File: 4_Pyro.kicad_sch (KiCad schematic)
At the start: 27 parts, among them J601 XT60-M, Q601 IRLZ44N, Q602 IRLZ44N, Q603 IRLZ44N, Q604 IRLZ44N, Q605 IRLZ44N, Q606 IRLZ44N, U601 PC817, U602 PC817, U603 PC817, U604 PC817, U605 PC817, U606 PC817

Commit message: Continued connections for the new NAV
Added continuity sensing through a 8:1 mux
Restructured schematic so that everything actually fits in page 4
Updated CubeMX (ioc) file with pinout
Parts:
- added R505, R506, R511, R512, R517, R518: 4k7, symbol Device:R
- added R519: 1k, symbol Device:R
- added U507: CD4051B, Package_SO:SOIC-16_3.9x9.9mm_P1.27mm, symbol Analog_Switch:CD4051B
- renumbered C601 to C501, D601 to D501, J601 to J501, Q605 to Q501, Q602 to Q502, Q603 to Q503, Q604 to Q504, Q601 to Q505, Q606 to Q506, R609 to R501, R602 to R502, R611 to R503, R604 to R504, R605 to R507, R606 to R508, R607 to R509, R608 to R510, R601 to R513, R610 to R514, R603 to R515, R612 to R516, U605 to U501, U602 to U502, U603 to U503, U604 to U504, U601 to U505, U606 to U506
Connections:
- net DROGUE_S1 is gone; now on net PYRO_0: U501.1
- net DROGUE_S2 is gone; now on net PYRO_1: U502.1
- net FIRE_S1 is gone; now on net PYRO_2: U503.1
- net FIRE_S2 is gone; now on net PYRO_3: U504.1
- net MAIN_S1 is gone; now on net PYRO_4: U505.1
- net GND: now also R519.2; no longer C501.2, D501.1 (A1)
- net DROGUE_1 renamed PYRO_0
- net PYRO_0: now also R505.1, R505.2, U507.13 (X0)
- net DROGUE_2 renamed PYRO_1
- net PYRO_1: now also R506.1, R506.2, U507.14 (X1)
- net FIRE_1 renamed PYRO_2
- net PYRO_2: now also R511.1, R511.2, U507.15 (X2)
- net FIRE_2 renamed PYRO_3
- net PYRO_3: now also R512.1, R512.2, U507.12 (X3)
- net MAIN_1 renamed PYRO_4
- net PYRO_4: now also R517.1, R517.2, U507.1 (X4)
- net MAIN_2 renamed PYRO_5
- net PYRO_5: now also R518.1, R518.2, U507.5 (X5)
- net MAIN_S2 renamed \PYRO_5
- new net +3.3V: U507.16 (VDD), U507.6 (INH)
- new net GND1: C501.2, D501.1 (A1)
- new net MUX_A: U507.11 (A)
- new net MUX_B: U507.10 (B)
- new net MUX_C: U507.9 (C)
- new net PYRO_SENSE: R519.1, U507.3 (X)
- no-connect marks 0 -> 2
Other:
- moved on the sheet: Q501, Q502, Q503, Q504, Q505, Q506, R501, R502, R503, R504, R507, R508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

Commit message: Finished restructuring schematic
Most components that were on page 3 are now in their own page
Added high-frequency 4.7 uF capacitor to servo power line
Continuity sensing on pyrochannels is multiplexed to one ADC on NAV.
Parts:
- added C502: 4u7, Capacitor_SMD:C_0603_1608Metric, symbol Device:C
- added R520: 4k7, Resistor_SMD:R_0603_1608Metric, symbol Device:R
- R505, R506, R511, R512, R517, R518, R519: footprint (none) -> Resistor_SMD:R_0603_1608Metric
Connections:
- net +3.3V: now also R520.1; no longer U507.6 (INH)
- net GND: now also Q502.2 (D), U507.7 (VEE), U507.8 (VSS); no longer Q502.3 (S)
- net GND1: now also C502.2
- net PYRO_0: no longer U501.1
- net PYRO_1: now also Q502.3 (S); no longer Q502.2 (D), U502.1
- net PYRO_2: no longer U503.1
- net PYRO_3: no longer U504.1
- net PYRO_4: no longer U505.1
- net SERVO_PWR: now also C502.1
- net \PYRO_5 renamed PYRO_S5
- new net PYRO_S0: U501.1
- new net PYRO_S1: U502.1
- new net PYRO_S2: U503.1
- new net PYRO_S3: U504.1
- new net PYRO_S4: U505.1
- new net ~{MUX_EN}: R520.2, U507.6 (INH)
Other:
- note added: "Pyrochannel 0"
- note added: "Pyrochannel 1"
- note added: "Pyrochannel 2"
- note added: "Pyrochannel 3"
- note added: "Pyrochannel 4"
- note added: "Pyrochannel 5"
- note added: "Pyrochannel Continuity Sensing"
- note removed: "Drogue Parachute Channel 1"
- note removed: "Drogue Parachute Channel 2"
- note removed: "Fire Channel 1"
- note removed: "Fire Channel 2"
- note removed: "Main Parachute Channel 1"
- note removed: "Main Parachute Channel 2"
- moved on the sheet: C501, D501, J501, Q501, R505, R519, U507

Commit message: Updated schematic so that servo GND and signal GND are no longer separate
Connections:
- net GND1 is gone; now on net GND: C501.2, C502.2, D501.1 (A1)
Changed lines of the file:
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@@
 		(color 0 0 0 0)
 	)
-	(junction
-		(at 198.12 156.21)
-		(diameter 0)
-		(color 0 0 0 0)
-	)
 	(no_connect
 		(at 53.34 158.75)
@@
 	)
 	(symbol
-		(lib_id "power:GND1")
-		(at 198.12 156.21 0)
-		(unit 1)
-		(body_style 1)
-		(exclude_from_sim no)
-		(in_bom yes)
-		(on_board yes)
-		(in_pos_files yes)
-		(dnp no)
-		(fields_autoplaced yes)
-		(property "Reference" "#PWR0504"
-			(at 198.12 162.56 0)
-			(hide yes)
-			(show_name no)
-			(do_not_autoplace no)
-			(effects
-				(font
-					(size 1.27 1.27)
-				)
-			)
-		)
-		(property "Value" "GND1"
-			(at 198.12 161.29 0)
-			(show_name no)
-			(do_not_autoplace no)
-			(effects
-				(font
-					(size 1.27 1.27)
-				)
-			)
-		)
-		(property "Footprint" ""
-			(at 198.12 156.21 0)
-			(hide yes)
-			(show_name no)
-			(do_not_autoplace no)
-			(effects
-				(font
-					(size 1.27 1.27)
-				)
-			)
-		)
-		(property "Datasheet" ""
-			(at 198.12 156.21 0)
-			(hide yes)
-			(show_name no)
-			(do_not_autoplace no)
-			(effects
-				(font
-					(size 1.27 1.27)
-				)
-			)
-		)
-		(property "Description" "Power symbol creates a global label with name \"GND1\" , ground"
-			(at 198.12 156.21 0)
-			(hide yes)
-			(show_name no)
-			(do_not_autoplace no)
-			(effects
-				(font
-					(size 1.27 1.27)
-				)
-			)
-		)
-		(pin "1"
-		)
-		(instances
-			(project "polaris"
-				(path "/cfb90e19-9fbe-47a1-a5ac-df522853d1d0/265a53e7-5f21-42fa-aa60-ebd8b846a247"
-					(reference "#PWR0504")
-					(unit 1)
-				)
-			)
-		)
-	)
-	(symbol
 		(lib_id "Device:R")
 		(at 144.78 67.31 0)
@@
 					(unit 1)
 				)
+			)
+		)
+	)
+	(symbol
+		(lib_id "power:GND")
+		(at 207.01 156.21 0)
+		(unit 1)
+		(body_style 1)
+		(exclude_from_sim no)
+		(in_bom yes)
+		(on_board yes)
+		(in_pos_files yes)
+		(dnp no)
+		(fields_autoplaced yes)
+		(property "Reference" "#PWR0504"
+			(at 207.01 162.56 0)
+			(hide yes)
+			(show_name no)
+			(do_not_autoplace no)
+			(effects
+				(font
+					(size 1.27 1.27)
+				)
+			)
+		)
+		(property "Value" "GND"
+			(at 207.01 161.29 0)
+			(show_name no)
+			(do_not_autoplace no)
+			(effects
+				(font
+					(size 1.27 1.27)
+				)
+			)
+		)
+		(property "Footprint" ""
+			(at 207.01 156.21 0)
+			(hide yes)
+			(show_name no)
+			(do_not_autoplace no)
+			(effects
+				(font
+					(size 1.27 1.27)
+				)
+			)
+		)
+		(property "Datasheet" ""
+			(at 207.01 156.21 0)
+			(hide yes)
+			(show_name no)
+			(do_not_autoplace no)
+			(effects
+				(font
+					(size 1.27 1.27)
+				)
+			)
+		)
+		(property "Description" "Power symbol creates a global label with name \"GND\" , ground"
+			(at 207.01 156.21 0)
+			(hide yes)
+			(show_name no)
+			(do_not_autoplace no)
+			(effects
+				(font
+					(size 1.27 1.27)
+				)
+			)
+		)
+		(pin "1"
+		)
+		(instances
+			(project "polaris"
+				(path "/cfb90e19-9fbe-47a1-a5ac-df522853d1d0/265a53e7-5f21-42fa-aa60-ebd8b846a247"
+					(reference "#PWR0504")
+					(unit 1)
+				)

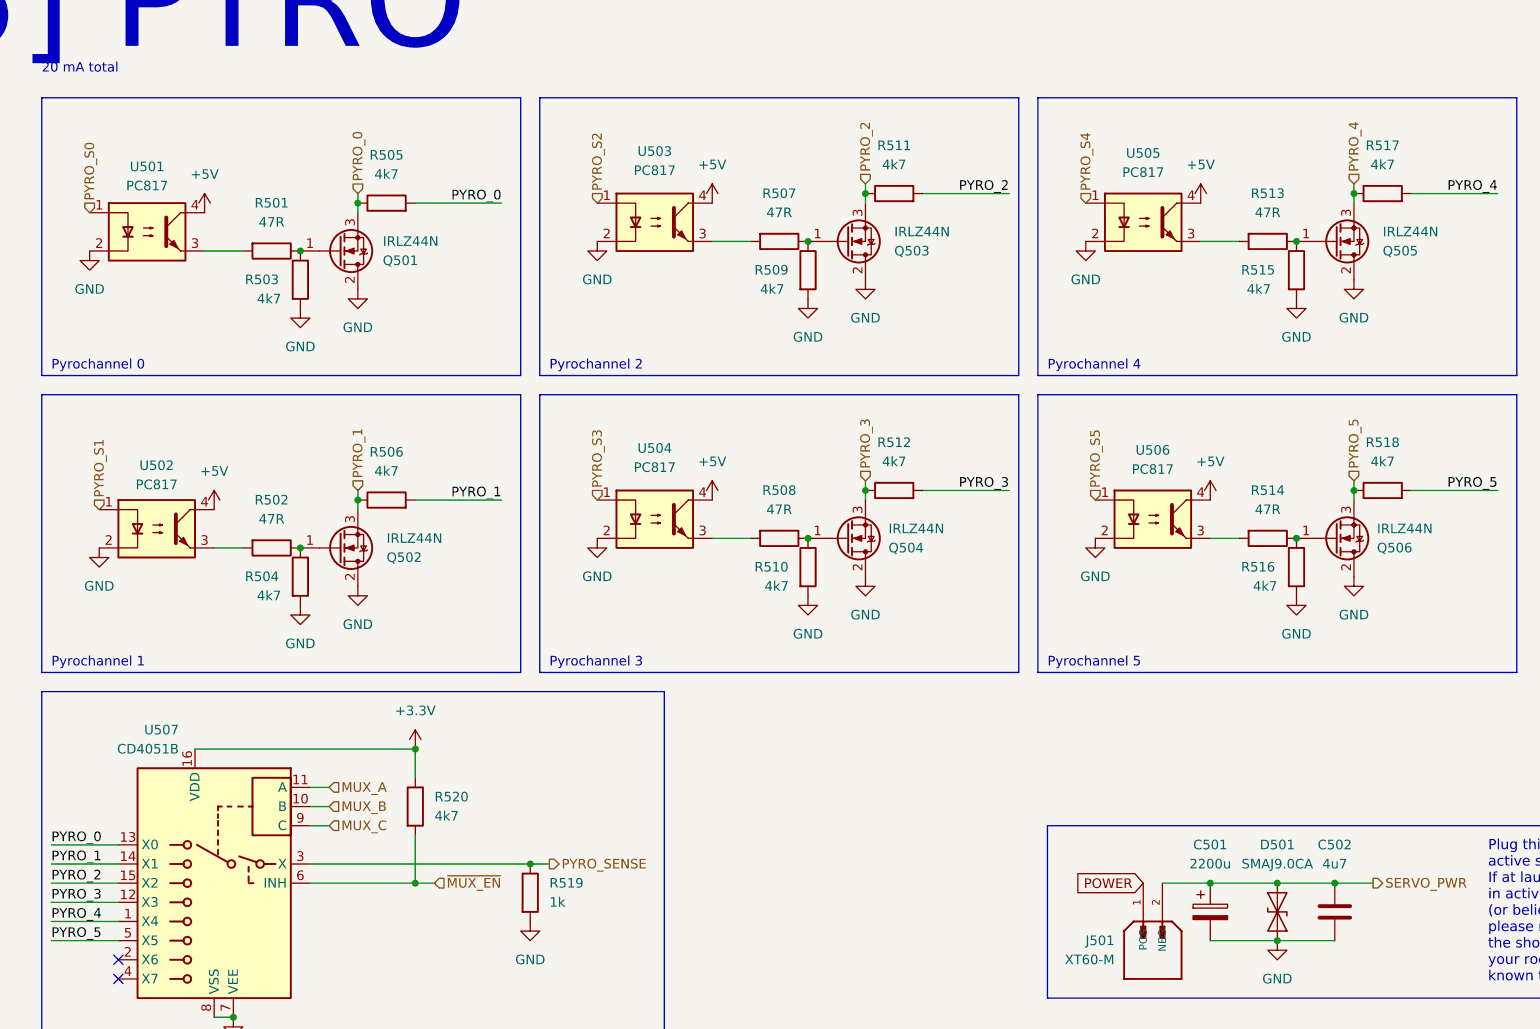
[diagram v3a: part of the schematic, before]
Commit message: Re-annotated schematic
Continued laying out traces on PCB
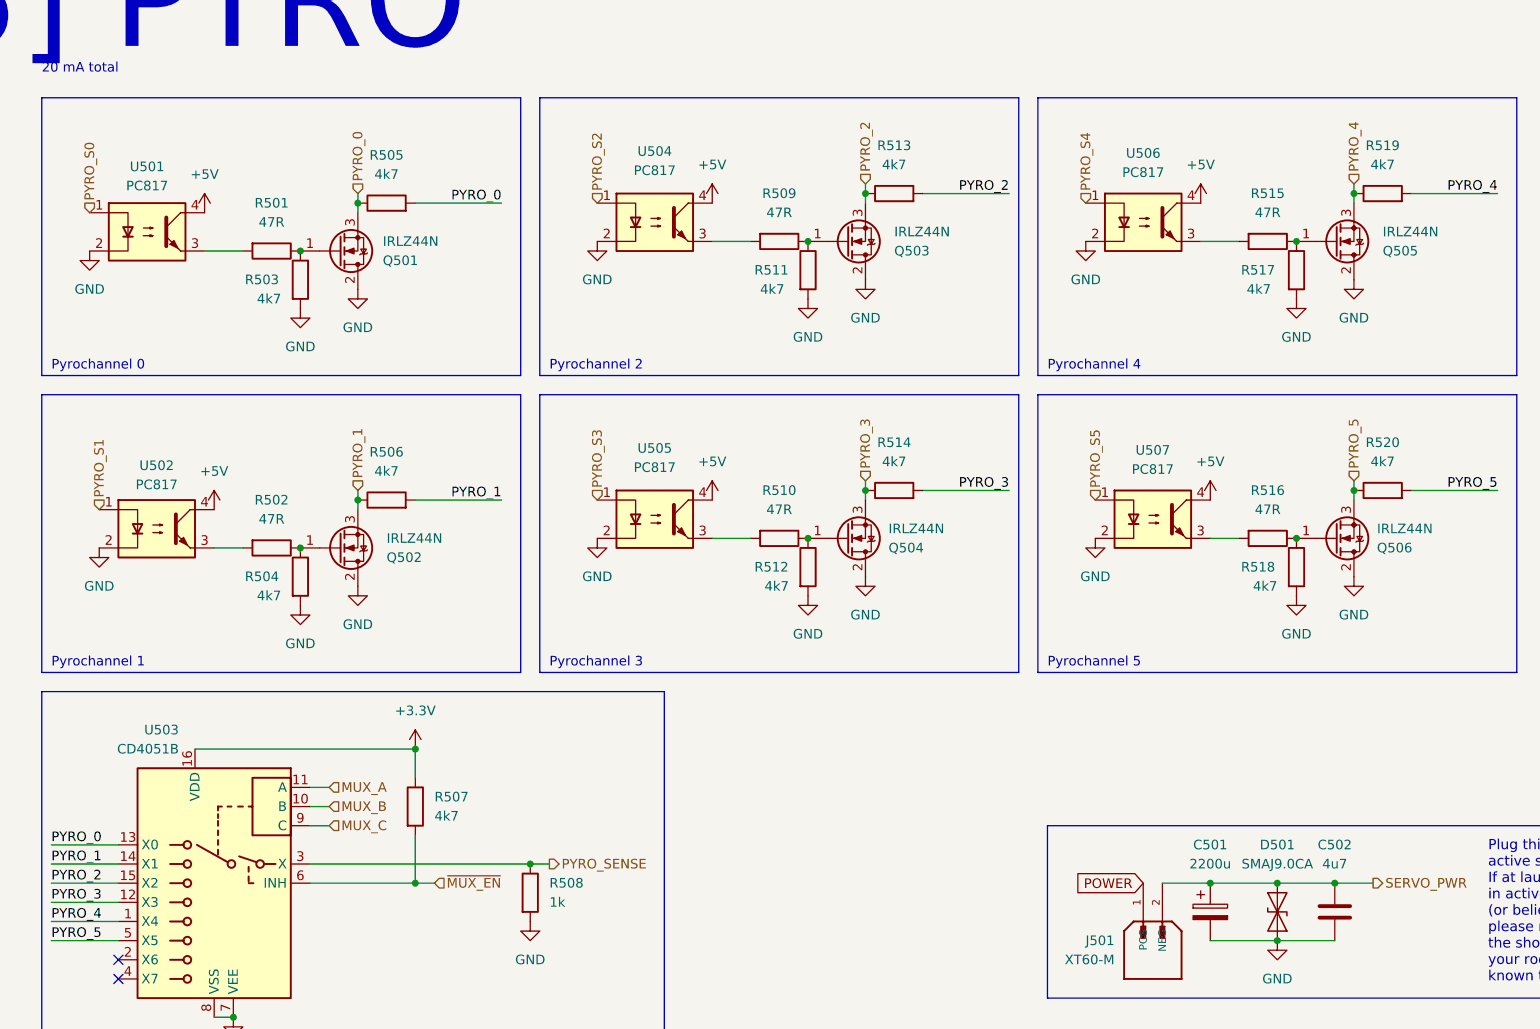
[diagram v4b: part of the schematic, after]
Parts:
- renumbered R520 to R507, R519 to R508, R507 to R509, R508 to R510, R509 to R511, R510 to R512, R511 to R513, R512 to R514, R513 to R515, R514 to R516, R515 to R517, R516 to R518, R517 to R519, R518 to R520, U507 to U503, U503 to U504, U504 to U505, U505 to U506, U506 to U507

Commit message: Re-annotated the whole page for no reason
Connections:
- net GND: now also Q501.3 (S), Q502.3 (S), Q503.3 (S), Q504.3 (S), Q505.3 (S), Q506.3 (S); no longer Q501.2 (D), Q502.2 (D), Q503.2 (D), Q504.2 (D), Q505.2 (D), Q506.2 (D)
- net PYRO_0: now also Q501.2 (D); no longer Q501.3 (S)
- net PYRO_1: now also Q502.2 (D); no longer Q502.3 (S)
- net PYRO_2: now also Q503.2 (D); no longer Q503.3 (S)
- net PYRO_3: now also Q504.2 (D); no longer Q504.3 (S)
- net PYRO_4: now also Q505.2 (D); no longer Q505.3 (S)
- net PYRO_5: now also Q506.2 (D); no longer Q506.3 (S)
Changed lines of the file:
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@@
 		(lib_id "Transistor_FET:IRLZ44N")
 		(at 149.86 102.87 0)
-		(mirror x)
 		(unit 1)
 		(body_style 1)
@@
 		(dnp no)
 		(property "Reference" "Q504"
-			(at 155.448 104.1401 0)
+			(at 155.448 101.5999 0)
 			(show_name no)
 			(do_not_autoplace no)
@@
 		)
 		(property "Value" "IRLZ44N"
-			(at 155.448 101.6001 0)
+			(at 155.448 104.1399 0)
 			(show_name no)
 			(do_not_autoplace no)
@@
 		)
 		(property "Footprint" "Package_TO_SOT_THT:TO-220-3_Vertical"
-			(at 154.94 100.965 0)
+			(at 154.94 104.775 0)
 			(hide yes)
 			(show_name no)
@@
 		)
 		(property "Datasheet" "http://www.irf.com/product-info/datasheets/data/irlz44n.pdf"
-			(at 154.94 99.06 0)
+			(at 154.94 106.68 0)
 			(hide yes)
 			(show_name no)
@@
 		(lib_id "Transistor_FET:IRLZ44N")
 		(at 214.63 63.5 0)
-		(mirror x)
 		(unit 1)
 		(body_style 1)
@@
 		(dnp no)
 		(property "Reference" "Q505"
-			(at 220.98 64.7701 0)
+			(at 220.98 62.2299 0)
 			(show_name no)
 			(do_not_autoplace no)
@@
 		)
 		(property "Value" "IRLZ44N"
-			(at 220.98 62.2301 0)
+			(at 220.98 64.7699 0)
 			(show_name no)
 			(do_not_autoplace no)
@@
 		)
 		(property "Footprint" "Package_TO_SOT_THT:TO-220-3_Vertical"
-			(at 219.71 61.595 0)
+			(at 219.71 65.405 0)
 			(hide yes)
 			(show_name no)
@@
 		)
 		(property "Datasheet" "http://www.irf.com/product-info/datasheets/data/irlz44n.pdf"
-			(at 219.71 59.69 0)
+			(at 219.71 67.31 0)
 			(hide yes)
 			(show_name no)
@@
 		(lib_id "Transistor_FET:IRLZ44N")
 		(at 82.55 104.14 0)
-		(mirror x)
 		(unit 1)
 		(body_style 1)
@@
 		(dnp no)
 		(property "Reference" "Q502"
-			(at 88.9 105.4101 0)
+			(at 88.9 102.8699 0)
 			(show_name no)
 			(do_not_autoplace no)
@@
 		)
 		(property "Value" "IRLZ44N"
-			(at 88.9 102.8701 0)
+			(at 88.9 105.4099 0)
 			(show_name no)
 			(do_not_autoplace no)
@@
 		)
 		(property "Footprint" "Package_TO_SOT_THT:TO-220-3_Vertical"
-			(at 87.63 102.235 0)
+			(at 87.63 106.045 0)
 			(hide yes)
 			(show_name no)
@@
 		)
 		(property "Datasheet" "http://www.irf.com/product-info/datasheets/data/irlz44n.pdf"
-			(at 87.63 100.33 0)
+			(at 87.63 107.95 0)
 			(hide yes)
 			(show_name no)
@@
 		(lib_id "Transistor_FET:IRLZ44N")
 		(at 82.55 64.77 0)
-		(mirror x)
 		(unit 1)
 		(body_style 1)
@@
 		(dnp no)
 		(property "Reference" "Q501"
-			(at 88.392 66.0401 0)
+			(at 88.392 63.4999 0)
 			(show_name no)
 			(do_not_autoplace no)
@@
 		)
 		(property "Value" "IRLZ44N"
-			(at 88.392 63.5001 0)
+			(at 88.392 66.0399 0)
 			(show_name no)
 			(do_not_autoplace no)
@@
 		)
 		(property "Footprint" "Package_TO_SOT_THT:TO-220-3_Vertical"
-			(at 87.63 62.865 0)
+			(at 87.63 66.675 0)
 			(hide yes)
 			(show_name no)
@@
 		)
 		(property "Datasheet" "http://www.irf.com/product-info/datasheets/data/irlz44n.pdf"
-			(at 87.63 60.96 0)
+			(at 87.63 68.58 0)
 			(hide yes)
 			(show_name no)
@@
 		(lib_id "Transistor_FET:IRLZ44N")
 		(at 149.86 63.5 0)
-		(mirror x)
 		(unit 1)
 		(body_style 1)
@@
 		(dnp no)
 		(property "Reference" "Q503"
-			(at 156.21 64.7701 0)
+			(at 156.21 62.2299 0)
 			(show_name no)
 			(do_not_autoplace no)
@@
 		)
 		(property "Value" "IRLZ44N"
-			(at 156.21 62.2301 0)
+			(at 156.21 64.7699 0)
 			(show_name no)
 			(do_not_autoplace no)
@@
 		)
 		(property "Footprint" "Package_TO_SOT_THT:TO-220-3_Vertical"
-			(at 154.94 61.595 0)
+			(at 154.94 65.405 0)
 			(hide yes)
 			(show_name no)
@@
 		)
 		(property "Datasheet" "http://www.irf.com/product-info/datasheets/data/irlz44n.pdf"
-			(at 154.94 59.69 0)
+			(at 154.94 67.31 0)
 			(hide yes)
 			(show_name no)
@@
 		(lib_id "Transistor_FET:IRLZ44N")
 		(at 214.63 102.87 0)
-		(mirror x)
 		(unit 1)
 		(body_style 1)
@@
 		(dnp no)
 		(property "Reference" "Q506"
-			(at 220.218 104.1401 0)
+			(at 220.218 101.5999 0)
 			(show_name no)
 			(do_not_autoplace no)
@@
 		)
 		(property "Value" "IRLZ44N"
-			(at 220.218 101.6001 0)
+			(at 220.218 104.1399 0)
 			(show_name no)
 			(do_not_autoplace no)
@@
 		)
 		(property "Footprint" "Package_TO_SOT_THT:TO-220-3_Vertical"
-			(at 219.71 100.965 0)
+			(at 219.71 104.775 0)
 			(hide yes)
 			(show_name no)
@@
 		)
 		(property "Datasheet" "http://www.irf.com/product-info/datasheets/data/irlz44n.pdf"
-			(at 219.71 99.06 0)
+			(at 219.71 106.68 0)
 			(hide yes)
 			(show_name no)

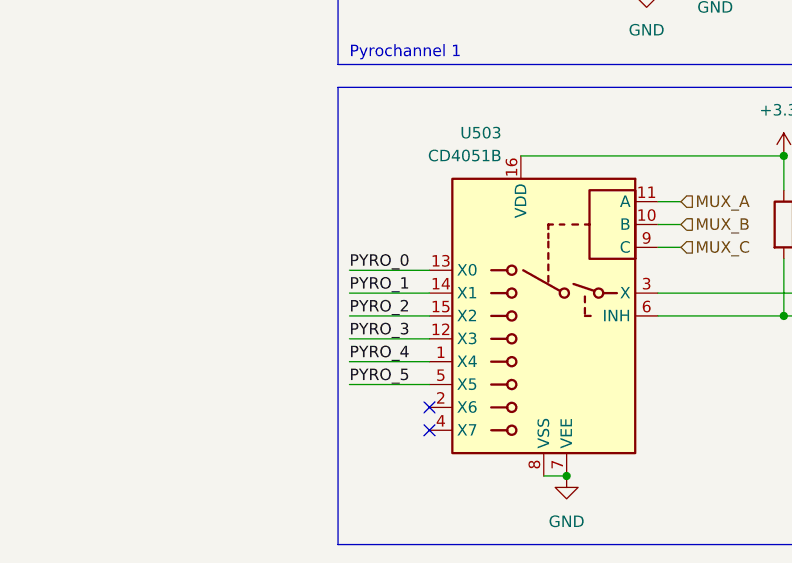
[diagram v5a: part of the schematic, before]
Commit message: Changed the board to support any telemetry radio
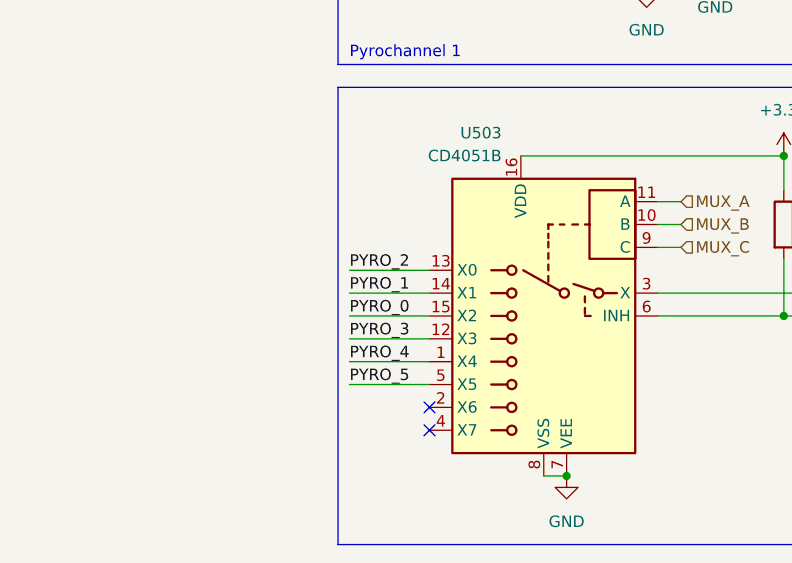
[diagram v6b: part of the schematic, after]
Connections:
- net PYRO_0: now also U503.15 (X2); no longer U503.13 (X0)
- net PYRO_2: now also U503.13 (X0); no longer U503.15 (X2)
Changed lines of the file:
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@@
 		)
 	)
-	(label "PYRO_0"
+	(label "PYRO_2"
 		(at 44.45 143.51 0)
 		(effects
@@
 		)
 	)
-	(label "PYRO_2"
+	(label "PYRO_0"
 		(at 44.45 148.59 0)
 		(effects
